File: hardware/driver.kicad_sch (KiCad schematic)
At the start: 10 parts, among them Q501 AO3400A

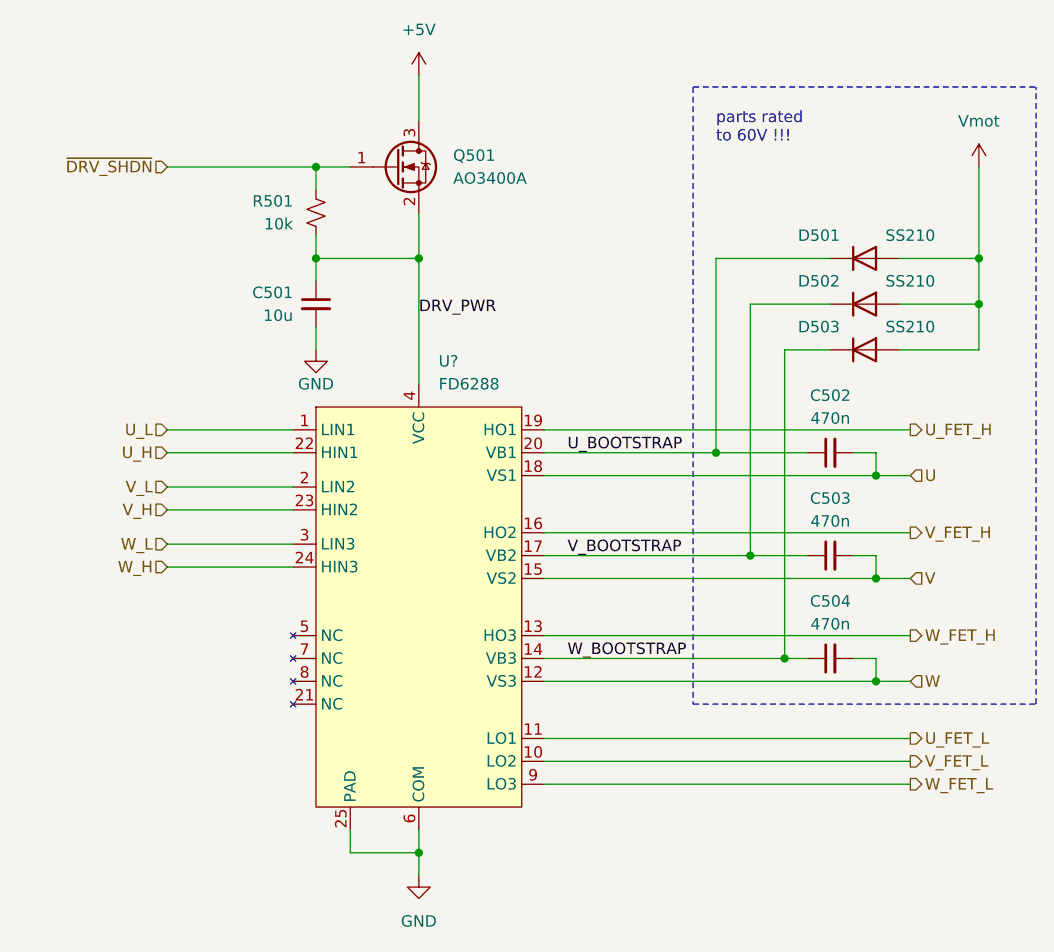
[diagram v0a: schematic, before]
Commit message: finish component selection
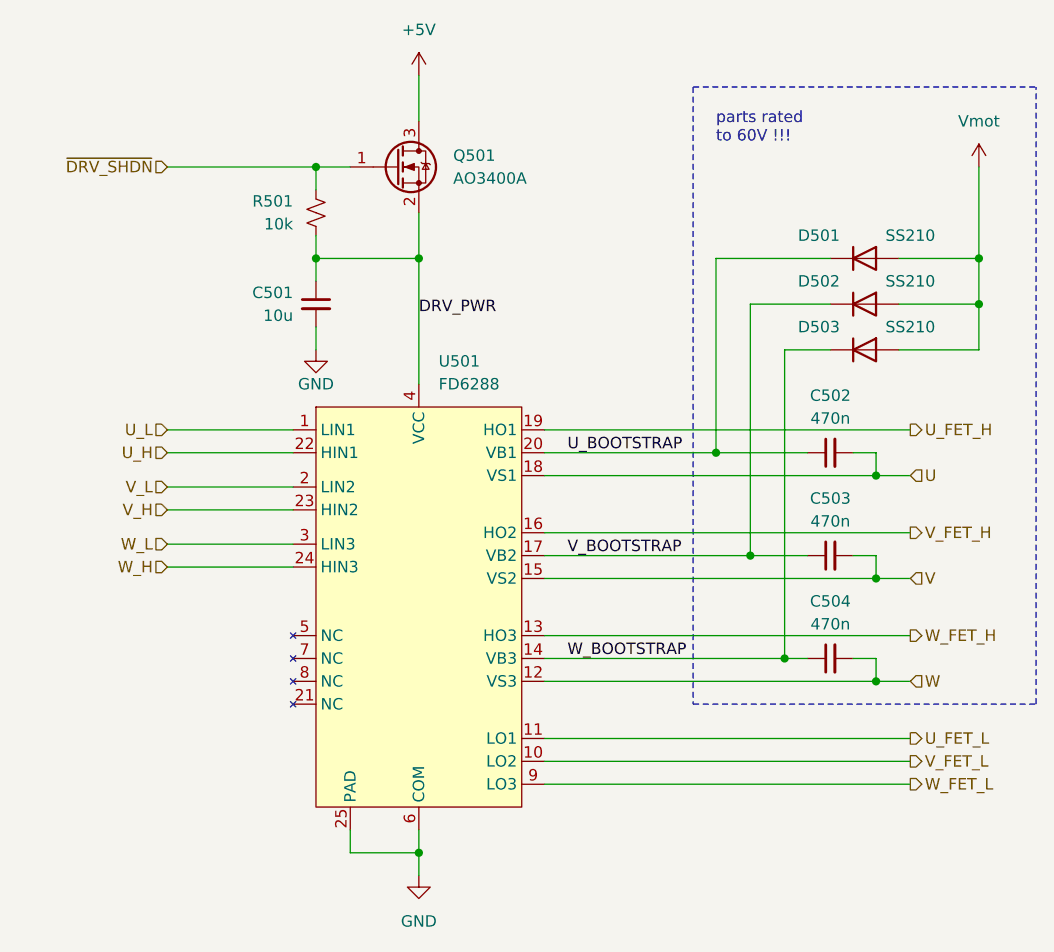
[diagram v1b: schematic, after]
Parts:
- Q501: LCSC Part (none) -> C20917
- gave numbers to parts that had none: 1
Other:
- company: (none) -> matei repair lab
- title: (none) -> GATE DRIVER
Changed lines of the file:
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@@
 (kicad_sch (version 20230121) (generator eeschema)
   (paper "A4")
+  (title_block
+    (title "GATE DRIVER")
+    (date "2023-10-11")
+    (rev "0.1")
+    (company "matei repair lab")
+  )
   (junction (at 187.96 68.58) (diameter 0) (color 0 0 0 0)
   )
@@
     (pin "2")
     (instances
-      (project "sfoc-stepper"
+      (project "lemon-pepper"
         (path "/0306e2fa-4433-4288-91d9-65a3484207ad/40d0f733-2cb2-4037-bc30-ae30111fe2e1"
           (reference "D502") (unit 1)
@@
     (pin "1")
     (instances
-      (project "sfoc-stepper"
+      (project "lemon-pepper"
         (path "/0306e2fa-4433-4288-91d9-65a3484207ad/40d0f733-2cb2-4037-bc30-ae30111fe2e1"
           (reference "#PWR0501") (unit 1)
@@
     (pin "1")
     (instances
-      (project "sfoc-stepper"
+      (project "lemon-pepper"
         (path "/0306e2fa-4433-4288-91d9-65a3484207ad/40d0f733-2cb2-4037-bc30-ae30111fe2e1"
           (reference "#PWR0503") (unit 1)
@@
     (pin "2")
     (instances
-      (project "sfoc-stepper"
+      (project "lemon-pepper"
         (path "/0306e2fa-4433-4288-91d9-65a3484207ad/40d0f733-2cb2-4037-bc30-ae30111fe2e1"
           (reference "C502") (unit 1)
@@
     (pin "2")
     (instances
-      (project "sfoc-stepper"
+      (project "lemon-pepper"
         (path "/0306e2fa-4433-4288-91d9-65a3484207ad/40d0f733-2cb2-4037-bc30-ae30111fe2e1"
           (reference "C503") (unit 1)
@@
   (symbol (lib_id "matei:FD6288") (at 125.73 99.06 0) (unit 1)
     (in_bom yes) (on_board yes) (dnp no) (fields_autoplaced)
-    (property "Reference" "U?" (at 127.9241 80.01 0)
+    (property "Reference" "U501" (at 127.9241 80.01 0)
       (effects (font (size 1.27 1.27)) (justify left))
     )
@@
     (pin "25")
     (instances
-      (project "sfoc-stepper"
-        (path "/0306e2fa-4433-4288-91d9-65a3484207ad/40d0f733-2cb2-4037-bc30-ae30111fe2e1"
-          (reference "U?") (unit 1)
+      (project "lemon-pepper"
+        (path "/0306e2fa-4433-4288-91d9-65a3484207ad/40d0f733-2cb2-4037-bc30-ae30111fe2e1"
+          (reference "U501") (unit 1)
         )
       )
@@
     (pin "2")
     (instances
-      (project "sfoc-stepper"
+      (project "lemon-pepper"
         (path "/0306e2fa-4433-4288-91d9-65a3484207ad/40d0f733-2cb2-4037-bc30-ae30111fe2e1"
           (reference "D503") (unit 1)
@@
       (effects (font (size 1.27 1.27)) (justify left) hide)
     )
+    (property "LCSC Part" "C20917" (at 123.19 58.42 0)
+      (effects (font (size 1.27 1.27)) hide)
+    )
     (pin "1")
     (pin "2")
     (pin "3")
     (instances
-      (project "sfoc-stepper"
+      (project "lemon-pepper"
         (path "/0306e2fa-4433-4288-91d9-65a3484207ad/40d0f733-2cb2-4037-bc30-ae30111fe2e1"
           (reference "Q501") (unit 1)
@@
     (pin "1")
     (instances
-      (project "sfoc-stepper"
+      (project "lemon-pepper"
         (path "/0306e2fa-4433-4288-91d9-65a3484207ad/40d0f733-2cb2-4037-bc30-ae30111fe2e1"
           (reference "#PWR0502") (unit 1)
@@
     (pin "2")
     (instances
-      (project "sfoc-stepper"
+      (project "lemon-pepper"
         (path "/0306e2fa-4433-4288-91d9-65a3484207ad/40d0f733-2cb2-4037-bc30-ae30111fe2e1"
           (reference "D501") (unit 1)
@@
     (pin "1")
     (instances
-      (project "sfoc-stepper"
+      (project "lemon-pepper"
         (path "/0306e2fa-4433-4288-91d9-65a3484207ad/40d0f733-2cb2-4037-bc30-ae30111fe2e1"
           (reference "#PWR0504") (unit 1)
@@
     (pin "2")
     (instances
-      (project "sfoc-stepper"
+      (project "lemon-pepper"
         (path "/0306e2fa-4433-4288-91d9-65a3484207ad/40d0f733-2cb2-4037-bc30-ae30111fe2e1"
           (reference "C504") (unit 1)
@@
     (pin "2")
     (instances
-      (project "sfoc-stepper"
+      (project "lemon-pepper"
         (path "/0306e2fa-4433-4288-91d9-65a3484207ad/40d0f733-2cb2-4037-bc30-ae30111fe2e1"
           (reference "C501") (unit 1)
@@
     (pin "2")
     (instances
-      (project "sfoc-stepper"
+      (project "lemon-pepper"
         (path "/0306e2fa-4433-4288-91d9-65a3484207ad/40d0f733-2cb2-4037-bc30-ae30111fe2e1"
           (reference "R501") (unit 1)
